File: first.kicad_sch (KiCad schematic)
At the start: 47 parts, among them J1 Conn_01x02_Socket, J10 Conn_01x02_Socket, J11 USB_C_Receptacle_USB2.0_16P, J12 Conn_01x03_Socket, J13 Conn_01x02_Socket, J14 Conn_01x02_Socket, J15 Conn_ST_STDC14, J2 Conn_01x03_Socket, J3 Conn_01x03_Socket, J4 Conn_01x03_Socket, J5 Conn_01x03_Socket, J6 Conn_01x03_Socket, J7 Conn_01x03_Socket, J8 Conn_01x03_Socket, SW1 SW_Push, SW3 SW_Wuerth_450301014042, U1 STM32F446RETx, U4 BD33FC0FP, U5 MCP2562-E-P

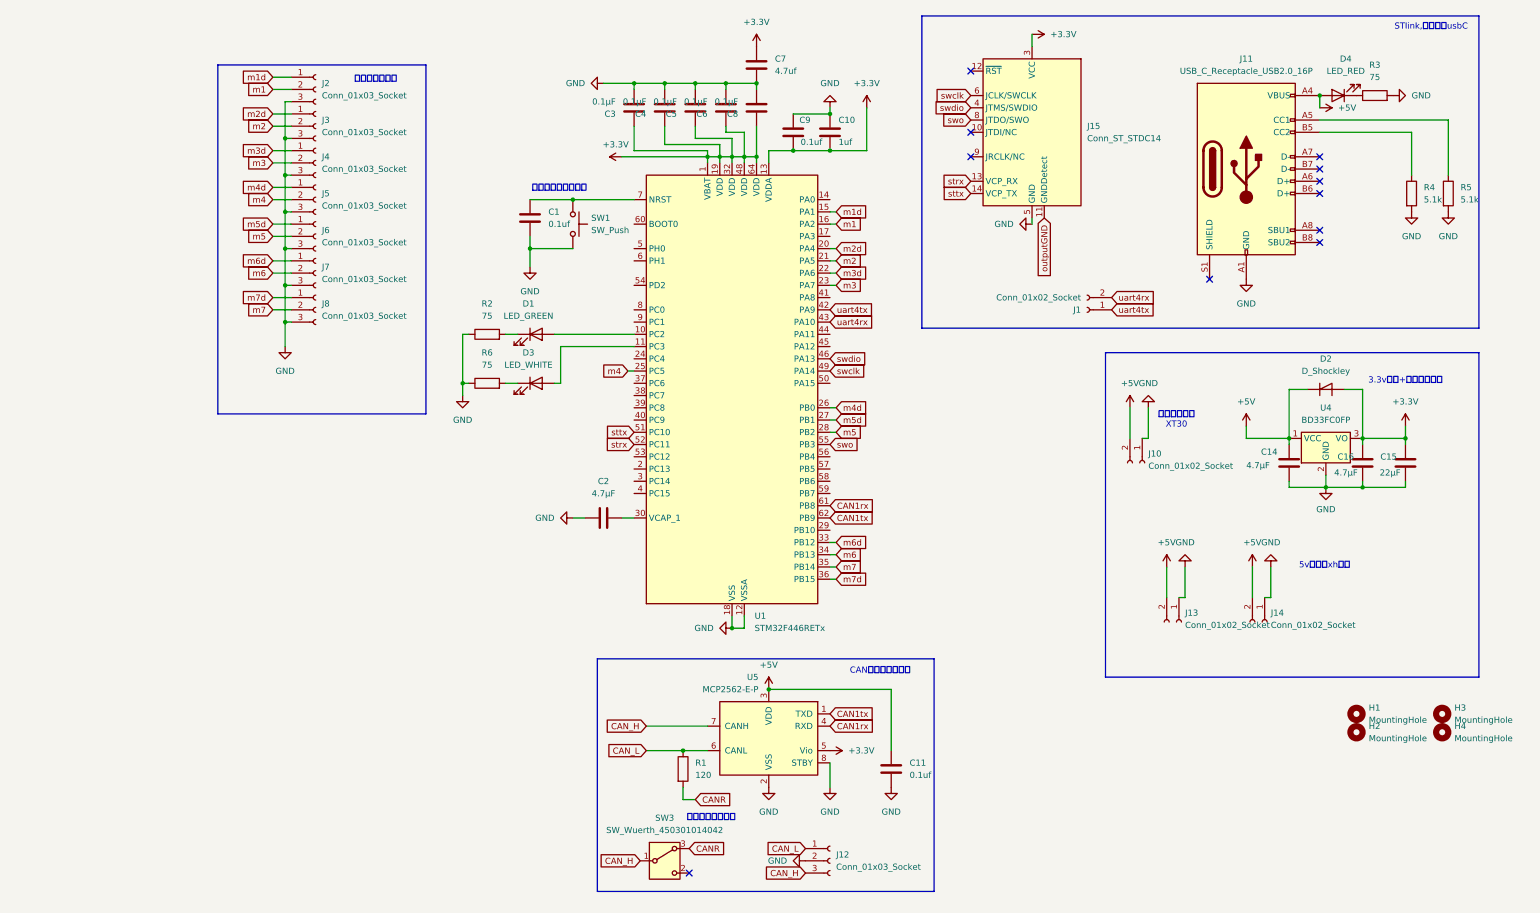
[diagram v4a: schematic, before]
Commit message: 回路図の微調整、pcbエディターでの配線、完成版ver1
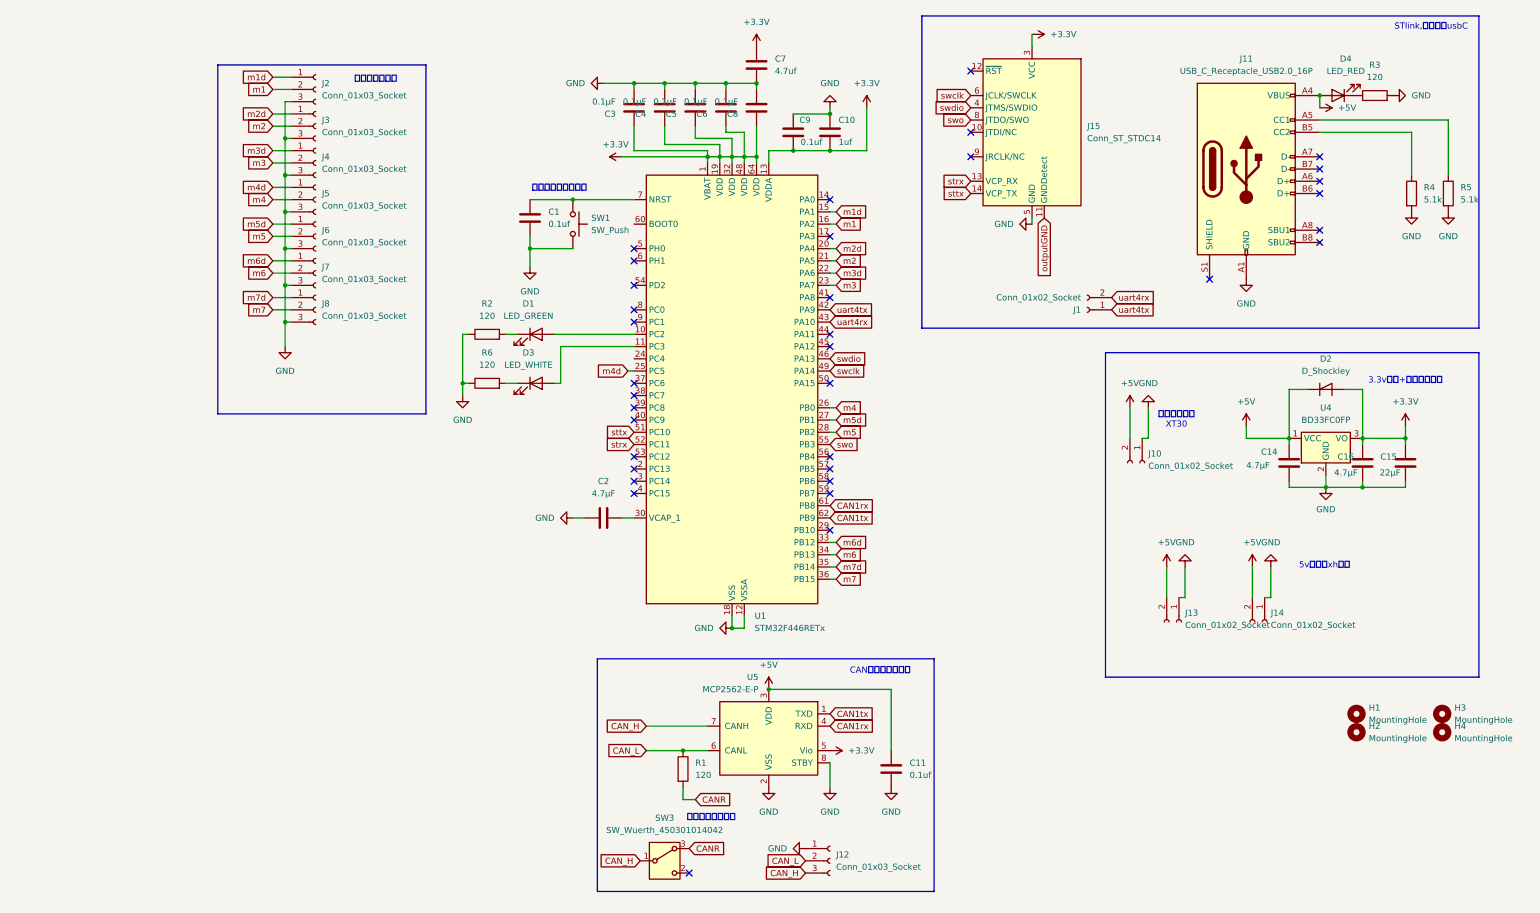
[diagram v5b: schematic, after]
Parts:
- R2, R3, R6: value 75 -> 120
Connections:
- net CAN_L: now also J12.2 (Pin_2); no longer J12.1 (Pin_1)
- net GND: now also J12.1 (Pin_1); no longer J12.2 (Pin_2)
- net m4: now also U1.26 (PB0); no longer U1.25 (PC5)
- net m4d: now also U1.25 (PC5); no longer U1.26 (PB0)
- net m7: now also U1.36 (PB15); no longer U1.35 (PB14)
- net m7d: now also U1.35 (PB14); no longer U1.36 (PB15)
- no-connect marks 11 -> 35

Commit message: PCBAの仕様に沿った部品に変更、再配置
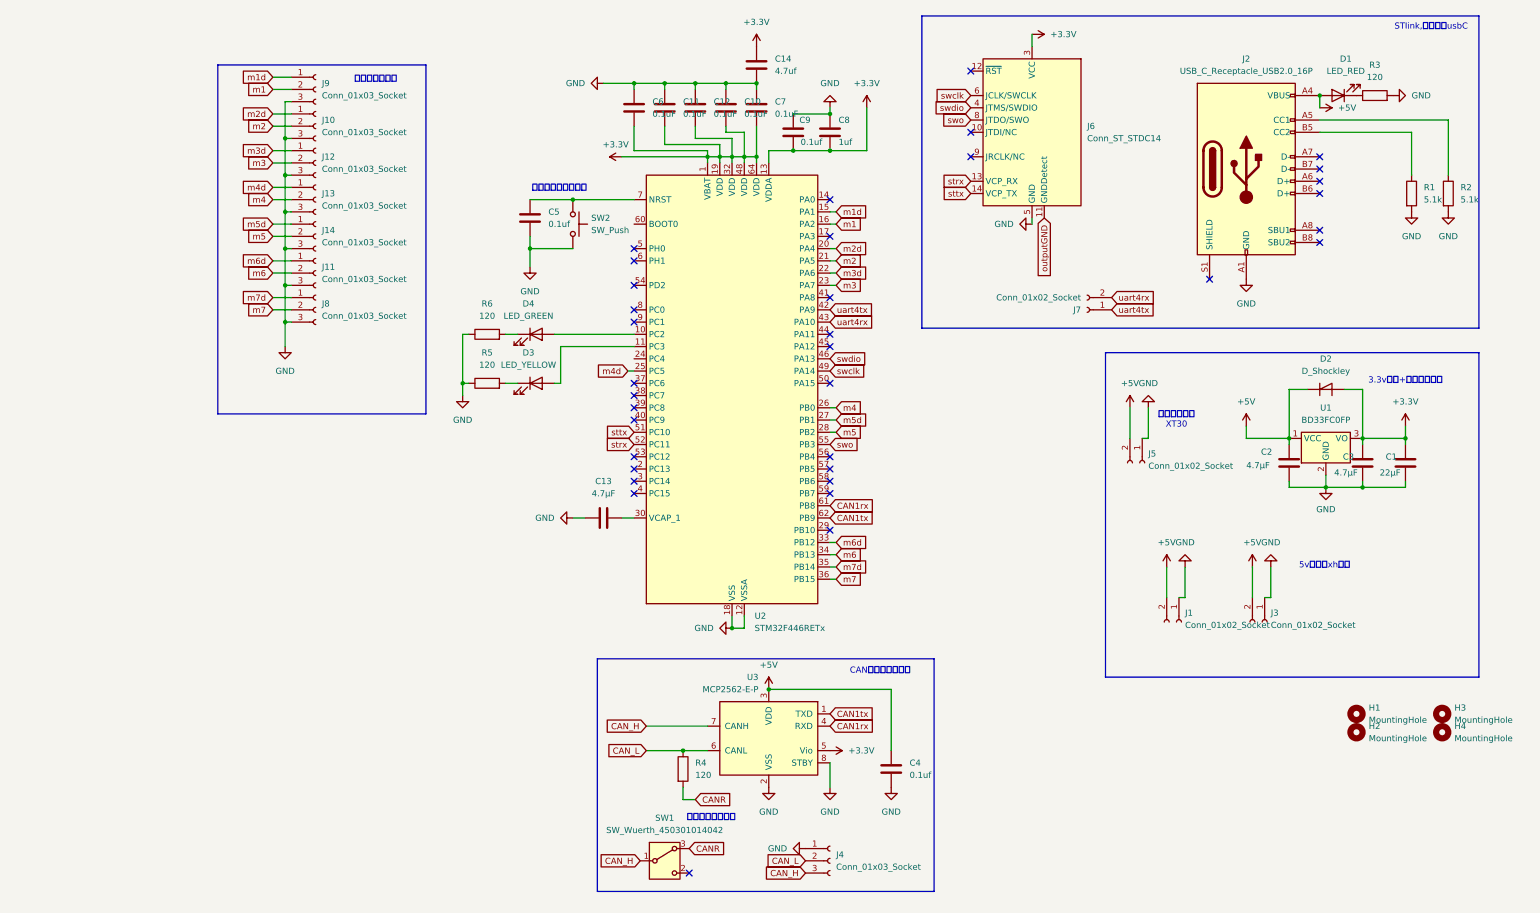
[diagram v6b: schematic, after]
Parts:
- C10: renamed from C6; value 0.1μF -> 0.1uF; footprint Capacitor_SMD:C_0201_0603Metric_Pad0.64x0.40mm_HandSolder -> Capacitor_SMD:C_0402_1005Metric_Pad0.74x0.62mm_HandSolder
- C11: renamed from C4; value 0.1μF -> 0.1uF; footprint Capacitor_SMD:C_0201_0603Metric_Pad0.64x0.40mm_HandSolder -> Capacitor_SMD:C_0402_1005Metric_Pad0.74x0.62mm_HandSolder
- C12: renamed from C5; value 0.1μF -> 0.1uF; footprint Capacitor_SMD:C_0201_0603Metric_Pad0.64x0.40mm_HandSolder -> Capacitor_SMD:C_0402_1005Metric_Pad0.74x0.62mm_HandSolder
- C6: renamed from C3; value 0.1μF -> 0.1uF; footprint Capacitor_SMD:C_0201_0603Metric_Pad0.64x0.40mm_HandSolder -> Capacitor_SMD:C_0402_1005Metric_Pad0.74x0.62mm_HandSolder
- C7: renamed from C8; value 0.1μF -> 0.1uF; footprint Capacitor_SMD:C_0201_0603Metric_Pad0.64x0.40mm_HandSolder -> Capacitor_SMD:C_0402_1005Metric_Pad0.74x0.62mm_HandSolder
- C9: footprint Capacitor_SMD:C_0201_0603Metric_Pad0.64x0.40mm_HandSolder -> Capacitor_SMD:C_0402_1005Metric_Pad0.74x0.62mm_HandSolder
- D1: renamed from D4; footprint Diode_SMD:D_0603_1608Metric_Pad1.05x0.95mm_HandSolder -> Diode_SMD:D_0805_2012Metric_Pad1.15x1.40mm_HandSolder
- D2: footprint Diode_SMD:D_SOD-882 -> Diode_SMD:D_SOD-323_HandSoldering
- D3: value LED_WHITE -> LED_YELLOW; footprint Diode_SMD:D_0603_1608Metric_Pad1.05x0.95mm_HandSolder -> Diode_SMD:D_0805_2012Metric_Pad1.15x1.40mm_HandSolder
- D4: renamed from D1; footprint Diode_SMD:D_0603_1608Metric_Pad1.05x0.95mm_HandSolder -> Diode_SMD:D_0805_2012Metric_Pad1.15x1.40mm_HandSolder
- R1: renamed from R4; footprint Resistor_SMD:R_1206_3216Metric_Pad1.30x1.75mm_HandSolder -> Resistor_SMD:R_0603_1608Metric_Pad0.98x0.95mm_HandSolder
- R2: renamed from R5; footprint Resistor_SMD:R_1206_3216Metric_Pad1.30x1.75mm_HandSolder -> Resistor_SMD:R_0603_1608Metric_Pad0.98x0.95mm_HandSolder
- R4: renamed from R1; footprint Resistor_SMD:R_0805_2012Metric_Pad1.20x1.40mm_HandSolder -> Resistor_SMD:R_0603_1608Metric_Pad0.98x0.95mm_HandSolder
- renumbered C15 to C1, C2 to C13, C7 to C14, C14 to C2, C16 to C3, C11 to C4, C1 to C5, C10 to C8, J13 to J1, J3 to J10, J7 to J11, J4 to J12, J5 to J13, J6 to J14, J11 to J2, J14 to J3, J12 to J4, J10 to J5, J15 to J6, J1 to J7, J2 to J9, R6 to R5, R2 to R6, SW3 to SW1, SW1 to SW2, U4 to U1, U1 to U2, U5 to U3

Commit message: stdc14のコネクタをきちんとしたものに取り換え、5V供給端子のループを解消
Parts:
- J6: footprint Connector_IDC:IDC-Header_2x07_P2.54mm_Vertical -> Connector_PinHeader_1.27mm:PinHeader_2x07_P1.27mm_Vertical
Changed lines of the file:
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@@
 			)
 		)
-		(property "Footprint" "Connector_IDC:IDC-Header_2x07_P2.54mm_Vertical"
+		(property "Footprint" "Connector_PinHeader_1.27mm:PinHeader_2x07_P1.27mm_Vertical"
 			(at 190.5 38.1 0)
 			(effects
